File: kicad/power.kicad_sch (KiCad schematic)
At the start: 17 parts, among them J8 Barrel_Jack_Switch_Pin3Ring, J9 Barrel_Jack_Switch_Pin3Ring, U5 L7809, U6 L7805

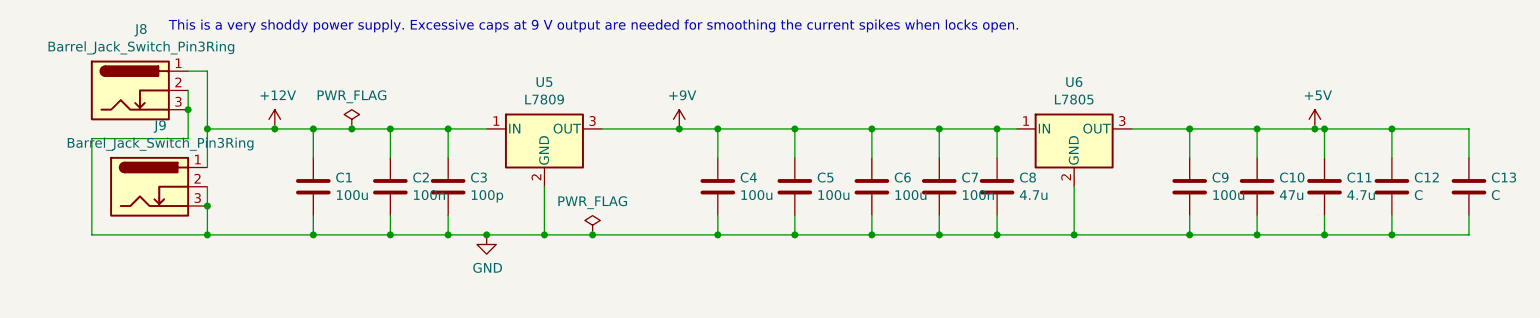
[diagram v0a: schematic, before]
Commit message: Update PCB with IO expander
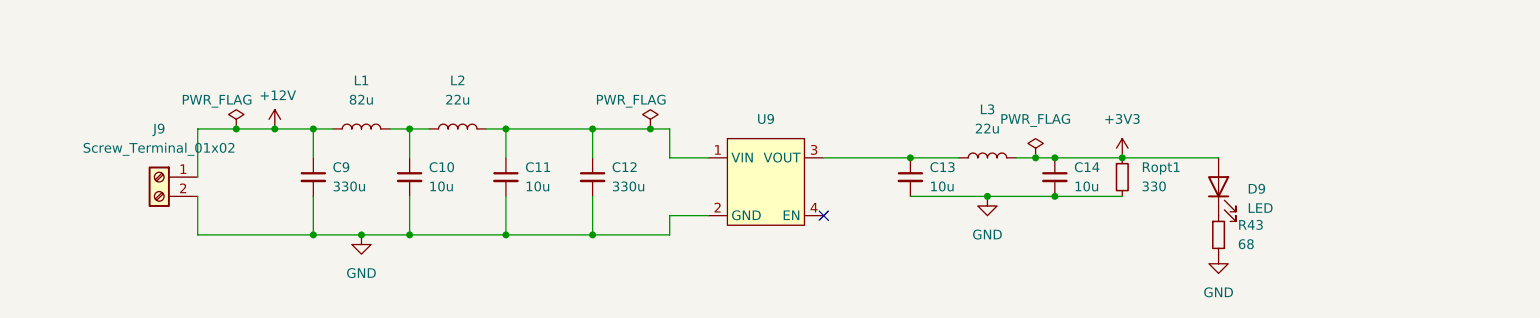
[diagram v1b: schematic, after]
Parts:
- removed C1, C4, C5, C6, C9: 100u, Capacitor_THT:CP_Radial_D5.0mm_P2.50mm, symbol Device:C
- removed C10: 47u, Capacitor_THT:CP_Radial_D5.0mm_P2.50mm, symbol Device:C
- removed C11: 4.7u, Capacitor_THT:CP_Radial_D5.0mm_P2.50mm, symbol Device:C
- removed C12, C13: C, Capacitor_SMD:C_0805_2012Metric_Pad1.15x1.40mm_HandSolder, symbol Device:C
- removed C2, C7: 100n, Capacitor_SMD:C_0805_2012Metric_Pad1.15x1.40mm_HandSolder, symbol Device:C
- removed C3: 100p, Capacitor_SMD:C_0805_2012Metric_Pad1.15x1.40mm_HandSolder, symbol Device:C
- removed C8: 4.7u, Capacitor_SMD:C_0805_2012Metric_Pad1.15x1.40mm_HandSolder, symbol Device:C
- removed J8: Barrel_Jack_Switch_Pin3Ring, Connector_BarrelJack:BarrelJack_CUI_PJ-102AH_Horizontal, symbol Connector:Barrel_Jack_Switch_Pin3Ring
- removed J9: Barrel_Jack_Switch_Pin3Ring, connectors:BarrelJack_CUI_PJ-102AH_Horizontal, symbol Connector:Barrel_Jack_Switch_Pin3Ring
- removed U5: L7809, Package_TO_SOT_THT:TO-220-3_Vertical, symbol Regulator_Linear:L7809
- removed U6: L7805, Package_TO_SOT_THT:TO-220-3_Vertical, symbol Regulator_Linear:L7805
- added C10, C11, C13, C14: 10u, Capacitor_THT:CP_Radial_D5.0mm_P2.50mm, symbol Device:C_Small
- added C12, C9: 330u, Capacitor_THT:CP_Radial_D8.0mm_P3.50mm, symbol Device:C_Small
- added D9: LED, LED_SMD:LED_PLCC-2_3x2mm_KA, symbol Device:LED
- added J9: Screw_Terminal_01x02, Connector_Phoenix_MSTB:PhoenixContact_MSTBA_2,5_2-G_1x02_P5.00mm_Horizontal, symbol Connector:Screw_Terminal_01x02
- added L1: 82u, Inductor_THT:L_Radial_D7.0mm_P3.00mm, symbol Device:L
- added L2, L3: 22u, Inductor_THT:L_Radial_D7.0mm_P3.00mm, symbol Device:L
- added R43: 68, Resistor_SMD:R_0805_2012Metric_Pad1.20x1.40mm_HandSolder, symbol Device:R_Small
- added Ropt1: 330, Resistor_SMD:R_0805_2012Metric_Pad1.20x1.40mm_HandSolder, symbol Device:R_Small
- added U9: ~, devkits:AMSROL-783, symbol devkits:AMSROL-783
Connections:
- net +12V: now also C9.1, J9.1 (Pin_1), L1.1
- net GND: now also C10.2, C11.2, C12.2, C13.2, C14.2, C9.2, J9.2 (Pin_2), R43.2, Ropt1.2, U9.2 (GND)
- new net: D9.1 (K), R43.1
- new net: C10.1, L1.2, L2.1
- new net: C13.1, L3.1, U9.3 (VOUT)
- new net: C11.1, C12.1, L2.2, U9.1 (VIN)
- new net +3V3: C14.1, D9.2 (A), L3.2, Ropt1.1
- no-connect marks 0 -> 1
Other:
- note removed: "This is a very shoddy power supply. Excessive caps at 9 V output are needed for smoothing the current spikes when locks open."
